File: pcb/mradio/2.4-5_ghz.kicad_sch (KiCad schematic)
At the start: 20 parts, among them J501 MDT420E01001, U502 SN74LVC1T45DRL

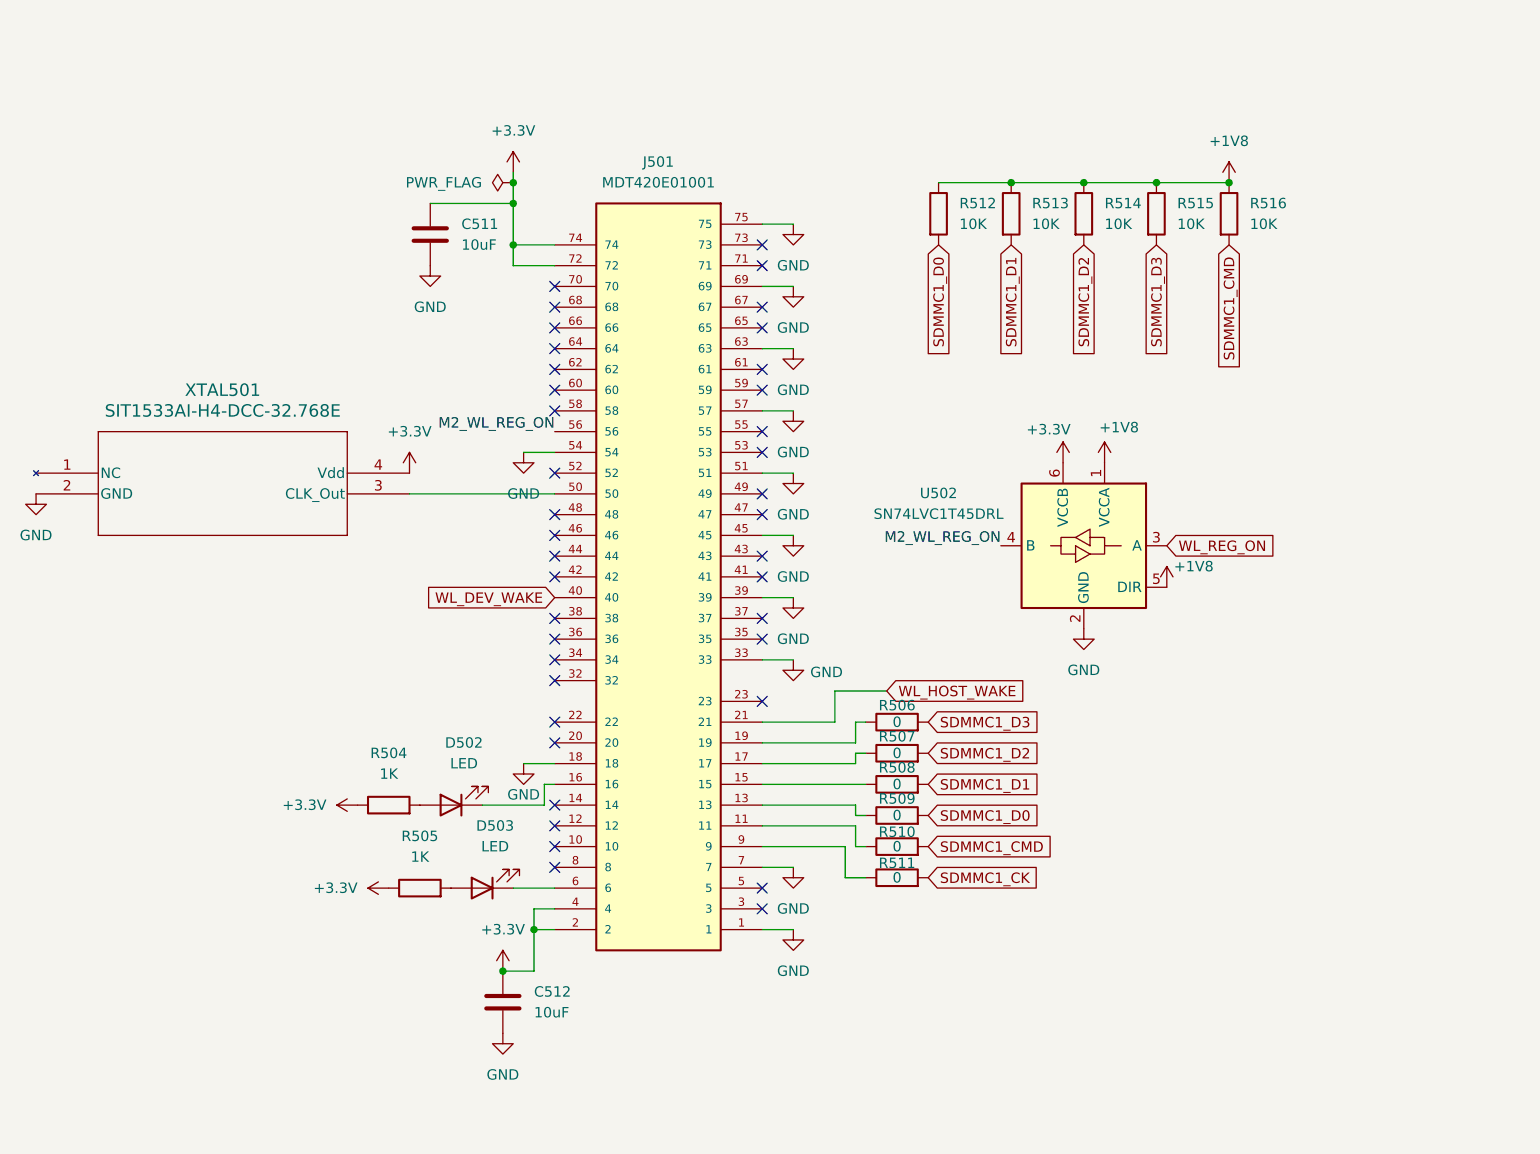
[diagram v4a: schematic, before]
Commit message: Add footprints, test points, unify 3v3
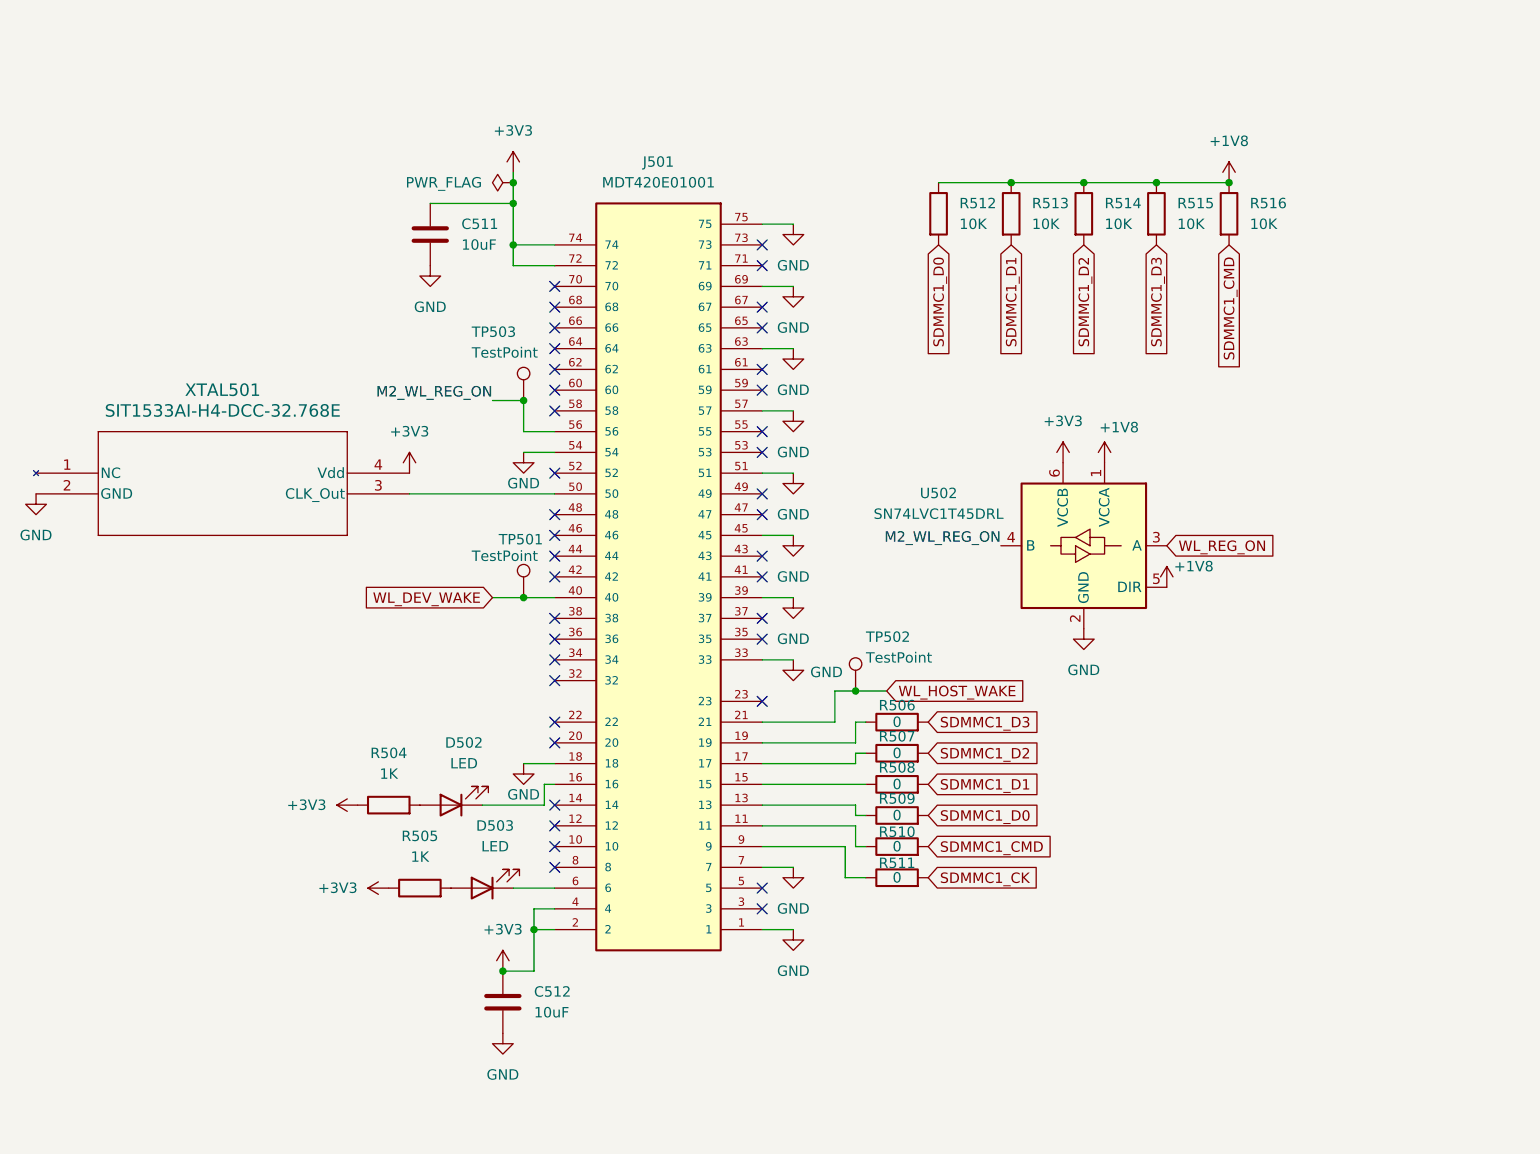
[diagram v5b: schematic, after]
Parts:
- added TP501, TP502, TP503: TestPoint, Package_DFN_QFN:Diodes_UDFN3810-9_TYPE_B, symbol Connector:TestPoint
- D502, D503: footprint (none) -> LED_SMD:LED_0603_1608Metric
- R506, R507, R508, R509, R510, R511: footprint (none) -> Resistor_SMD:R_0603_1608Metric
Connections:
- net M2_WL_REG_ON: now also TP503.1
- net WL_DEV_WAKE: now also TP501.1
- net WL_HOST_WAKE: now also TP502.1
- net +3.3V renamed +3V3

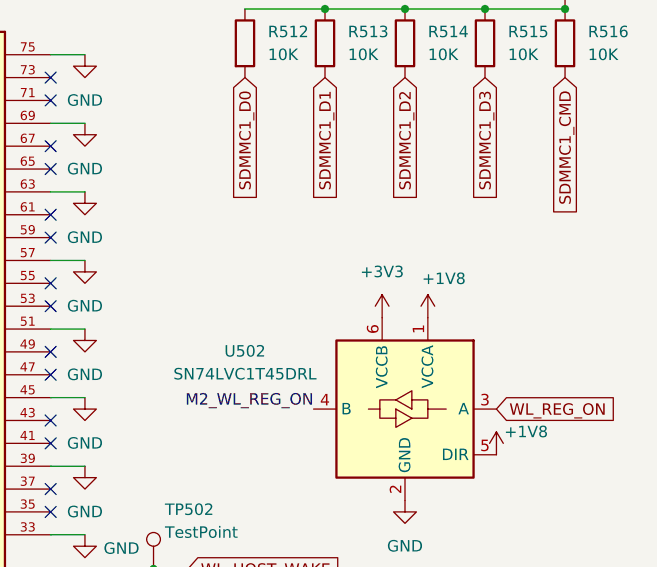
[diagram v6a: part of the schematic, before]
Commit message: add bypass caps to level shifters
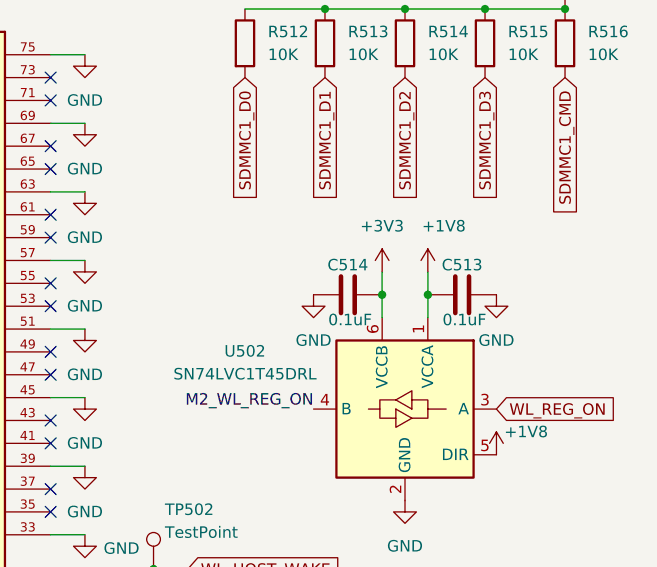
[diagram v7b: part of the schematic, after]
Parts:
- added C513, C514: 0.1uF, Capacitor_SMD:C_0603_1608Metric, symbol Device:C
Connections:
- net +1V8: now also C513.1
- net +3V3: now also C514.2
- net GND: now also C513.2, C514.1
